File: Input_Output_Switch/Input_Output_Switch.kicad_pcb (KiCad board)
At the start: 4 copper layers, 96.5 x 37.5 mm, 81 parts, among them J1 RV, J2 AudioJackIn, J3 AudioJackOut, J4 Barrel_Jack_Switch, J5 Gain, J8 PWR, Q1 MMBF4393LT1G, Q2 PZT2222A, Q3 MMBF4393LT1G, Q4 PZT2222A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

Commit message: Final version 1.0 ordered
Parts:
- C10, C11, C12, C13, C14, C15, C16: footprint Capacitor_SMD:C_0805_2012Metric -> Capacitor_SMD:C_0603_1608Metric_Pad1.08x0.95mm_HandSolder
- J1: value RV -> B3B-XH-A; footprint Connector_PinHeader_2.54mm:PinHeader_1x03_P2.54mm_Horizontal -> Connector_JST:JST_XH_B3B-XH-A_1x03_P2.50mm_Vertical; moved to F.Cu
- J2: value AudioJackIn -> A-6730
- J3: value AudioJackOut -> A-6730
- J4: value Barrel_Jack_Switch -> A-4118
- J8: value PWR -> B3B-XH-A; footprint Connector_PinHeader_2.54mm:PinHeader_1x03_P2.54mm_Vertical -> Connector_JST:JST_XH_B3B-XH-A_1x03_P2.50mm_Vertical
- Q2, Q4: value PZT2222A -> 2N4401D75ZCT-ND; footprint Package_TO_SOT_SMD:SOT-23 -> Package_TO_SOT_THT:TO-92_Inline_Wide
- U1: value TL072 -> 296-TL072HIDRCT-ND
- moved TPG2 31.1 mm to (174.9, 75.0)
- moved J8 5.08 mm to (150.0, 67.4), turned to 180 degrees
- moved J1 3.72 mm to (201.5, 93.4), turned to 0 degrees
- moved Q2 3.20 mm to (150.7, 88.7), turned to 0 degrees
- moved TP9 2.74 mm to (178.4, 75.0)
- moved Q4 1.92 mm to (163.4, 88.6), turned to 0 degrees
- moved R14 1.91 mm to (148.1, 88.3)
- moved R19 1.91 mm to (171.0, 88.3)
- moved R15 0.64 mm to (158.3, 88.3)
- moved R20 0.38 mm to (161.1, 88.3)
- turned C14 to -90 degrees
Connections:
- Q2 pad 1: Net-(Q2-B) -> GNDA
- Q2 pad 2: Net-(D4-K) -> Net-(Q2-B)
- Q2 pad 3: GNDA -> Net-(D4-K)
- Q4 pad 1: Net-(Q4-B) -> GNDA
- Q4 pad 2: Net-(Q4-C) -> Net-(Q4-B)
- Q4 pad 3: GNDA -> Net-(Q4-C)
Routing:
- net /P1: track 80.2 -> 84.2 mm
- net Net-(Q4-B): track 26.1 -> 29.2 mm, vias 3 -> 1
- net GNDA: track 27.3 -> 24.4 mm, vias 29 -> 14
- net Net-(R14-Pad2): track 11.4 -> 14.0 mm, vias 2 -> 0
- net /P2: track 74.3 -> 76.8 mm
- net Net-(Q4-C): track 18.2 -> 20.1 mm, vias 0 -> 2
- net Net-(D4-K): track 30.6 -> 32.3 mm, vias 0 -> 1
- net VCC/2: track 162.3 -> 160.5 mm
- net /jfet_footswitch/VOUT: track 10.5 -> 9.18 mm
- net /jfet_footswitch/SWOUT: track 32.7 -> 33.8 mm
- net VCC: track 38.4 -> 37.7 mm
- net Net-(Q2-B): vias 2 -> 0
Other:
- board text added: "JM: EQ8-Main-Board, v1.0, 2024/11/23"
- board text added: "S"
- board text added: "VC2"

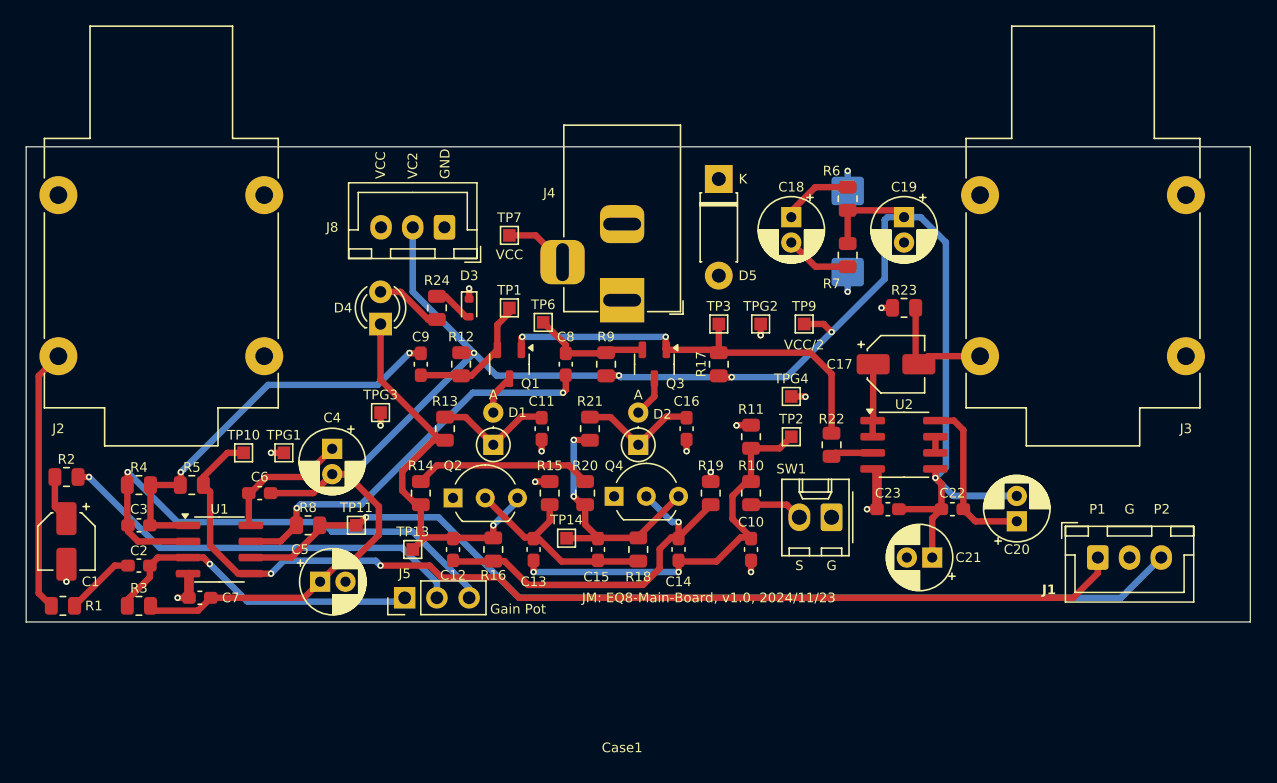
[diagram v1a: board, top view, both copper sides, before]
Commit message: Fix bypass resistor, add missing Vcc. Move to Kicad-9
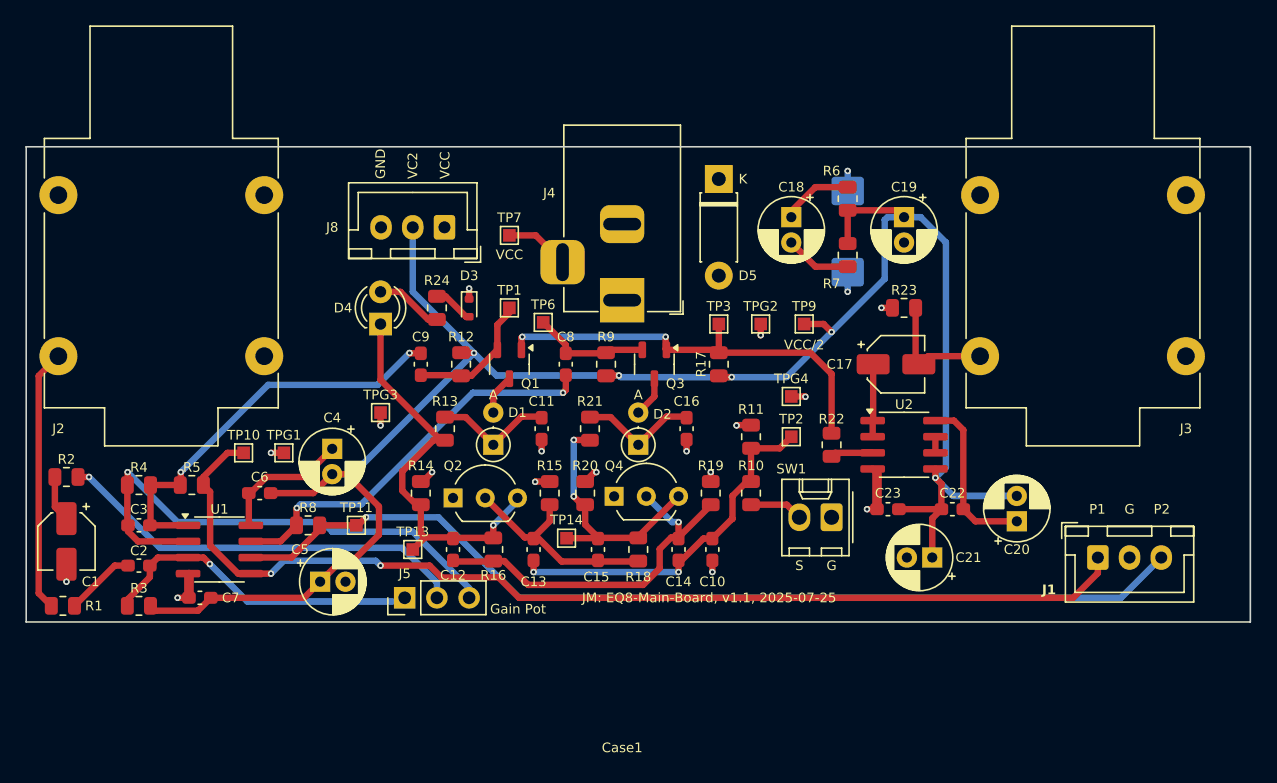
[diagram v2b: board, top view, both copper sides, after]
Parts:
- D1, D2: value 1N914 -> 1N914/1N4148
- moved C10 3.05 mm to (171.1, 92.8)
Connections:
- R14 pad 2: Net-(R14-Pad2) -> VCC
- R20 pad 2: Net-(R14-Pad2) -> VCC
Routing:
- net Net-(R14-Pad2): track 14.0 -> 0.00 mm
- net /jfet_footswitch/SW: track 31.6 -> 28.7 mm
- net VCC: track 37.7 -> 40.1 mm, vias 3 -> 5
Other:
- board text added: "${COMPANY}: ${TITLE}, ${REVISION}, ${ISSUE_DATE}"
- board text removed: "JM: EQ8-Main-Board, v1.0, 2024/11/23"
